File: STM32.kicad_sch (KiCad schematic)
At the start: 19 parts, among them IC1 TCAN3413DRBR, SW3 SW_SPDT, SW4 SW_Push, SW5 SW_SPDT, U1 STM32F072RBH6

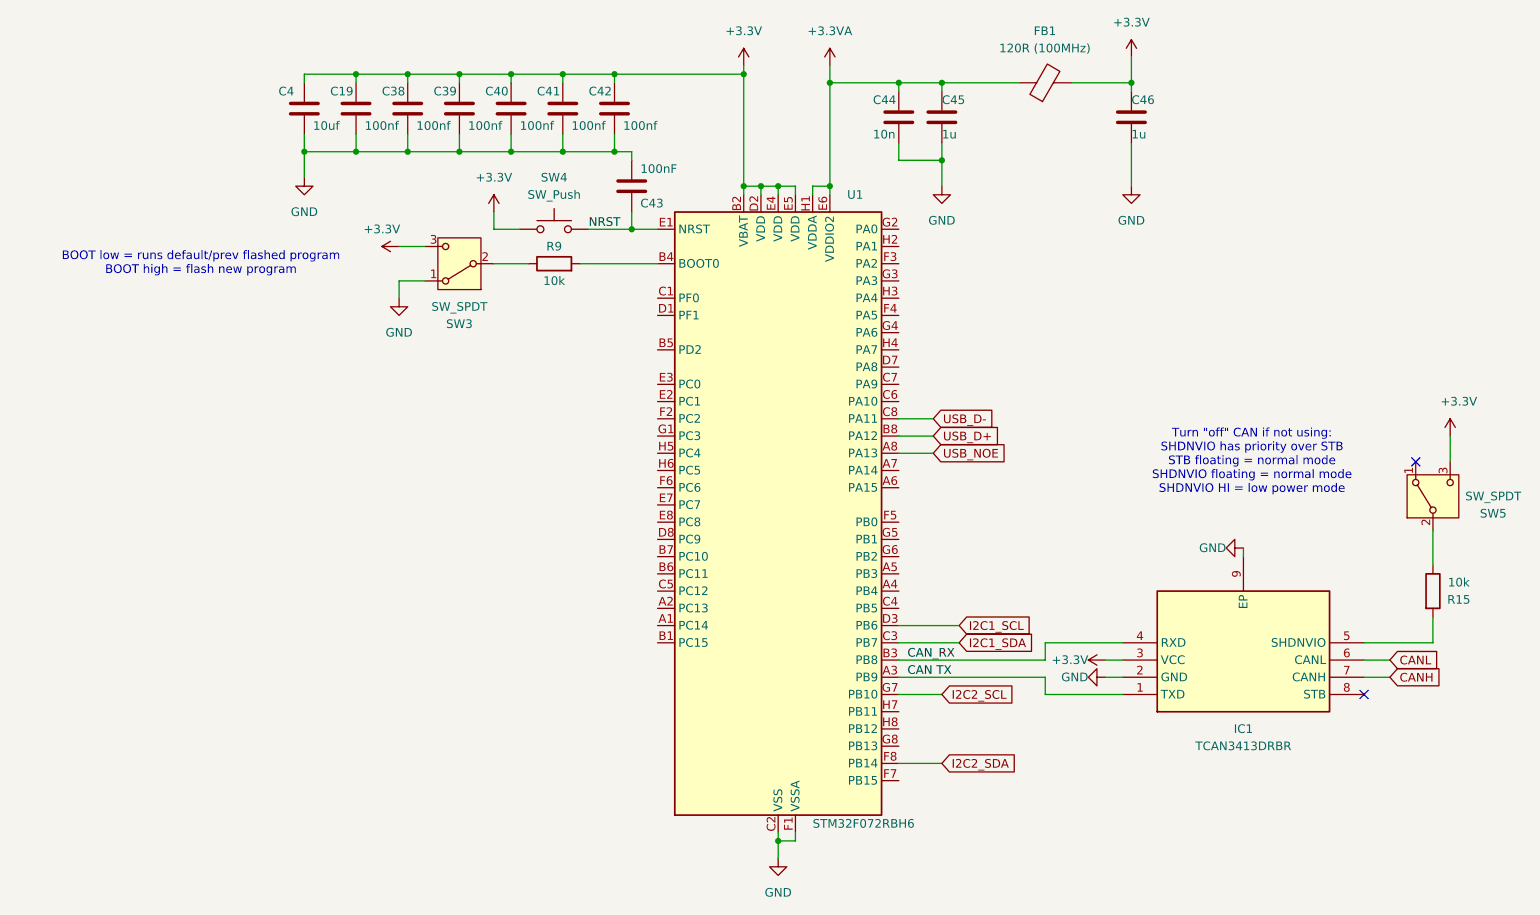
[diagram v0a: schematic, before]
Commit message: 3.3V changes and changed labels to hierarchical one's
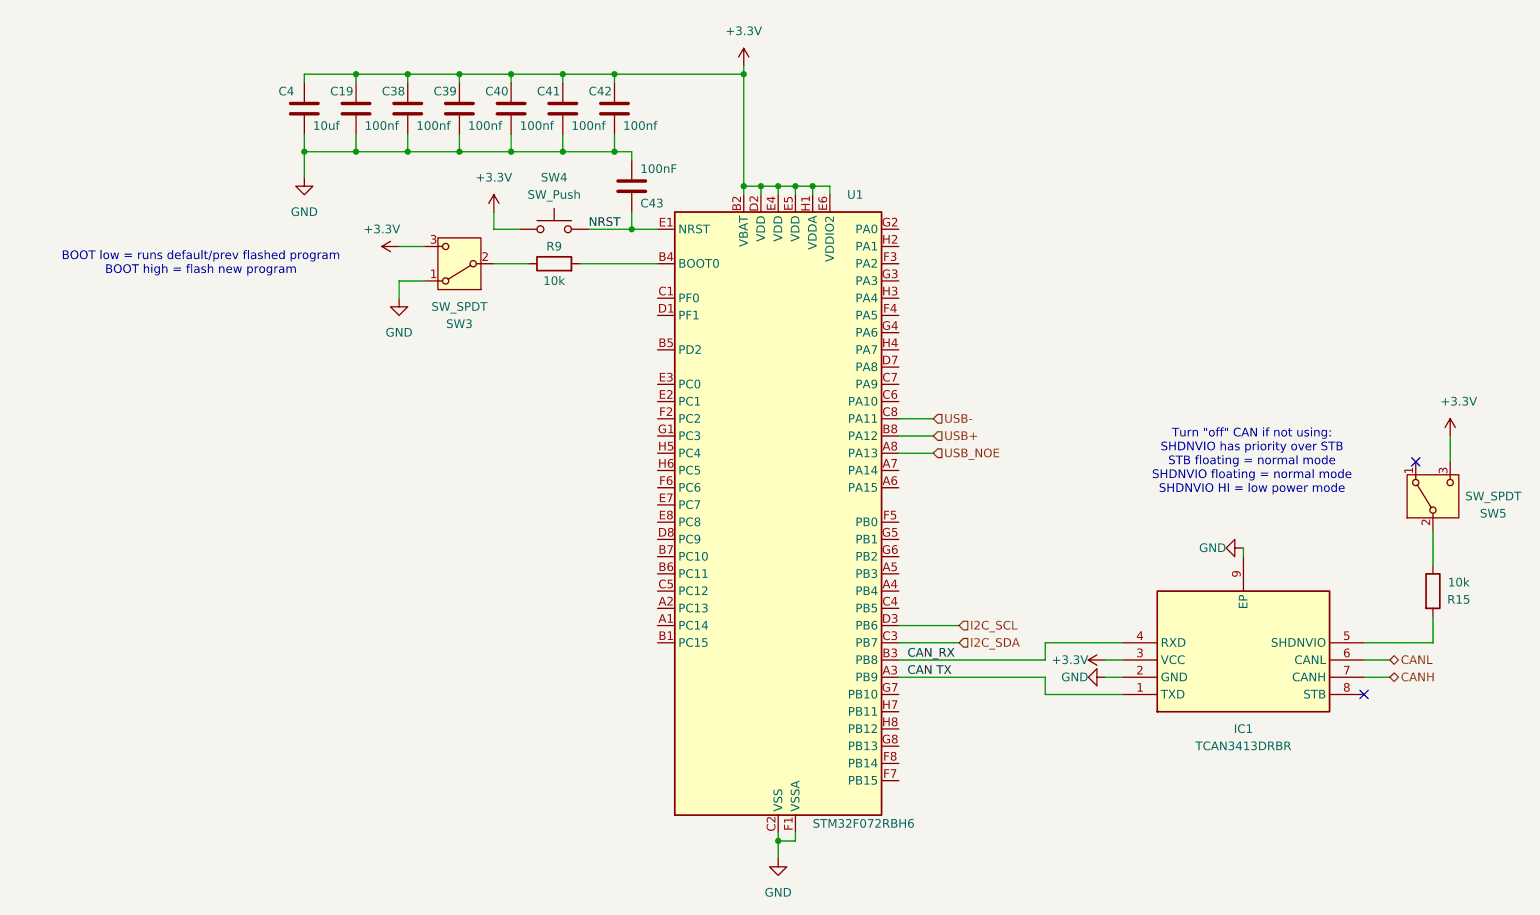
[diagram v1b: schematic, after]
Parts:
- removed C44: 10n, symbol Device:C
- removed C45, C46: 1u, symbol Device:C
- removed FB1: 120R (100MHz), symbol Device:FerriteBead
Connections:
- net +3.3VA is gone; now on net +3.3V: U1.E6 (VDDIO2), U1.H1 (VDDA)
- net I2C1_SCL renamed I2C_SCL
- net I2C1_SDA renamed I2C_SDA
- net I2C2_SCL: no longer names the net of U1.G7 (PB10)
- net I2C2_SDA: no longer names the net of U1.F8 (PB14)
- net USB_D+ renamed USB+
- net USB_D- renamed USB-

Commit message: linked everything together. still need to add capacitors
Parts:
- removed SW5: SW_SPDT, symbol Switch:SW_SPDT
- added D7: LED, symbol Device:LED
- added R17: 330, symbol Device:R_US
- R15, R9: symbol Device:R -> Device:R_US
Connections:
- net GND: now also D7.1 (K)
- net at U1.F5 (PB0): now also R15.1
- net USB_NOE: no longer names the net of U1.A8 (PA13)
- net USB_NOE: now also R17.2
- new net: D7.2 (A), R17.1
- no-connect marks 2 -> 1

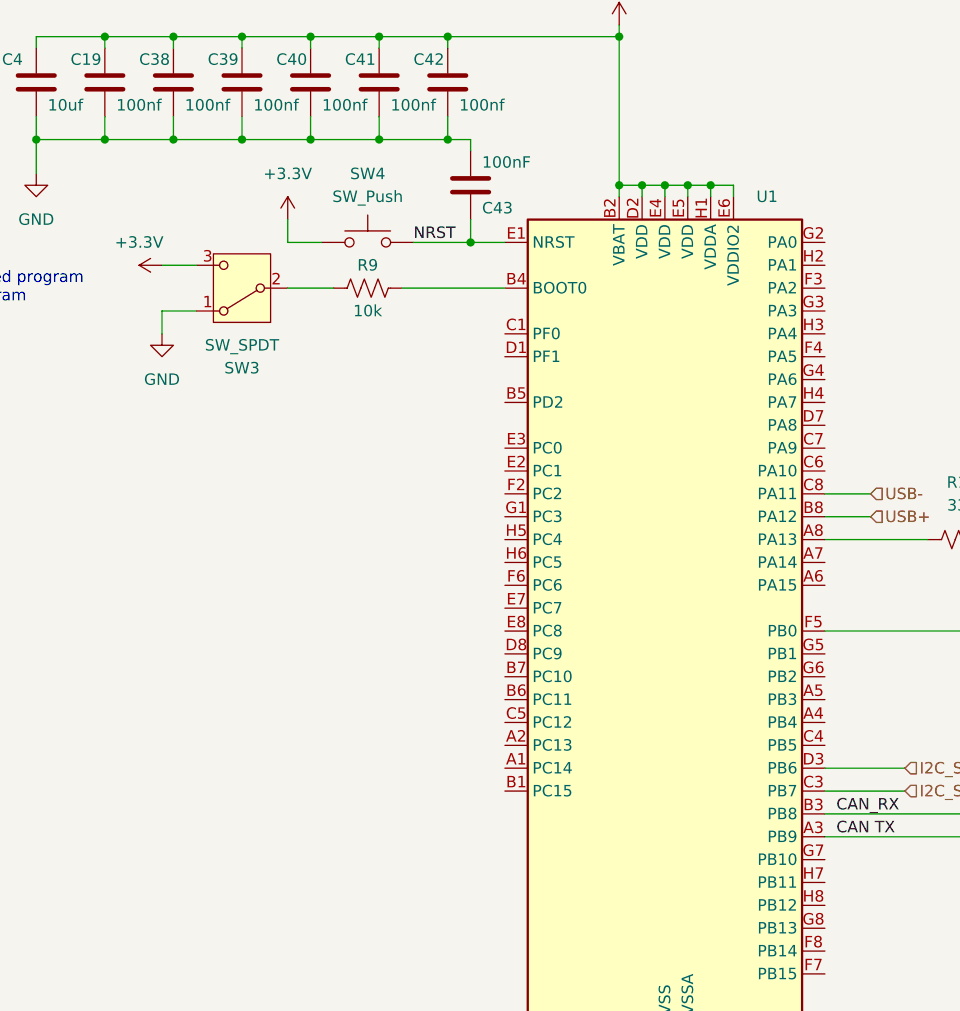
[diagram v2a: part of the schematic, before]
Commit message: started pcb layout, host and usbhub done
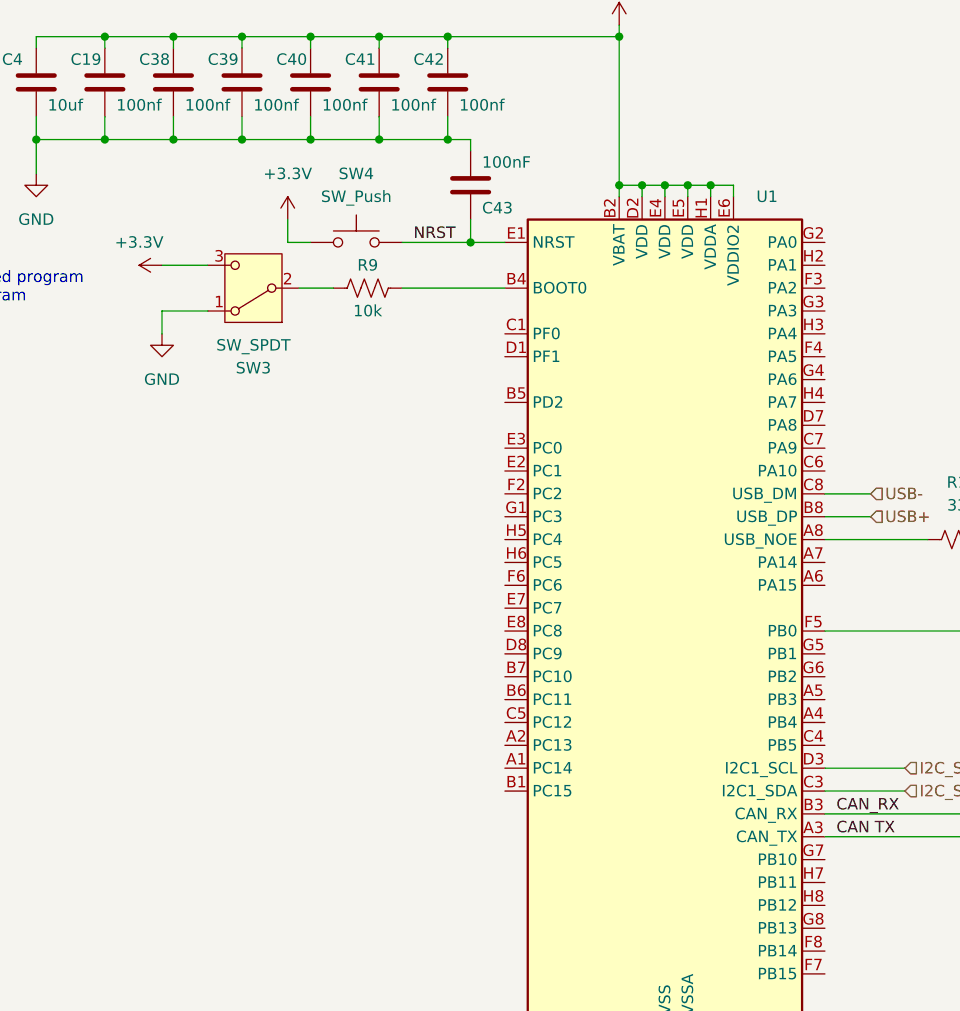
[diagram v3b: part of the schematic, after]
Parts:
- C19, C38, C39, C4, C40, C41, C42, C43: footprint (none) -> Capacitor_SMD:C_0603_1608Metric
- D7: footprint (none) -> LED_SMD:LED_0603_1608Metric
- R15, R17, R9: footprint (none) -> Resistor_SMD:R_0603_1608Metric
- SW3: footprint (none) -> Button_Switch_SMD:SW_SPDT_PCM12
- SW4: footprint (none) -> Button_Switch_SMD:SW_Push_1P1T_XKB_TS-1187A
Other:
- moved on the sheet: SW3, SW4
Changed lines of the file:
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@@
 	(wire
 		(pts
-			(xy 132.08 64.77) (xy 137.16 64.77)
+			(xy 133.35 64.77) (xy 137.16 64.77)
 		)
 		(stroke
@@
 	(wire
 		(pts
-			(xy 118.11 62.23) (xy 121.92 62.23)
+			(xy 118.11 62.23) (xy 123.19 62.23)
 		)
 		(stroke
@@
 	(wire
 		(pts
-			(xy 135.89 59.69) (xy 132.08 59.69)
+			(xy 134.62 59.69) (xy 132.08 59.69)
 		)
 		(stroke
@@
 	(wire
 		(pts
-			(xy 118.11 67.31) (xy 121.92 67.31)
+			(xy 118.11 67.31) (xy 123.19 67.31)
 		)
 		(stroke
@@
 	(wire
 		(pts
-			(xy 146.05 59.69) (xy 152.4 59.69)
+			(xy 144.78 59.69) (xy 152.4 59.69)
 		)
 		(stroke
@@
 		)
 		(pin "A3"
+			(alternate "CAN_TX")
 		)
 		(pin "F3"
@@
 		)
 		(pin "C3"
+			(alternate "I2C1_SDA")
 		)
 		(pin "G6"
@@
 		)
 		(pin "B8"
+			(alternate "USB_DP")
 		)
 		(pin "C2"
 		)
 		(pin "A8"
+			(alternate "USB_NOE")
 		)
 		(pin "C4"
@@
 		)
 		(pin "C8"
+			(alternate "USB_DM")
 		)
 		(pin "C7"
 		)
 		(pin "D3"
+			(alternate "I2C1_SCL")
 		)
 		(pin "E1"
@@
 		)
 		(pin "B3"
+			(alternate "CAN_RX")
 		)
 		(pin "A2"
@@
 			)
 		)
-		(property "Footprint" ""
+		(property "Footprint" "Capacitor_SMD:C_0603_1608Metric"
 			(at 105.1052 45.72 0)
 			(effects
@@
 	(symbol
 		(lib_id "Switch:SW_Push")
-		(at 140.97 59.69 0)
+		(at 139.7 59.69 0)
 		(unit 1)
 		(exclude_from_sim no)
@@
 		(fields_autoplaced yes)
 		(property "Reference" "SW4"
-			(at 140.97 52.07 0)
+			(at 139.7 52.07 0)
 			(effects
 				(font
@@
 		)
 		(property "Value" "SW_Push"
-			(at 140.97 54.61 0)
-			(effects
-				(font
-					(size 1.27 1.27)
-				)
-			)
-		)
-		(property "Footprint" ""
-			(at 140.97 54.61 0)
+			(at 139.7 54.61 0)
+			(effects
+				(font
+					(size 1.27 1.27)
+				)
+			)
+		)
+		(property "Footprint" "Button_Switch_SMD:SW_Push_1P1T_XKB_TS-1187A"
+			(at 139.7 54.61 0)
 			(effects
 				(font
@@
 		)
 		(property "Datasheet" "~"
-			(at 140.97 54.61 0)
+			(at 139.7 54.61 0)
 			(effects
 				(font
@@
 		)
 		(property "Description" "Push button switch, generic, two pins"
-			(at 140.97 59.69 0)
+			(at 139.7 59.69 0)
 			(effects
 				(font
@@
 			)
 		)
-		(property "Footprint" ""
+		(property "Footprint" "LED_SMD:LED_0603_1608Metric"
 			(at 214.63 92.71 0)
 			(effects
@@
 			)
 		)
-		(property "Footprint" ""
+		(property "Footprint" "Resistor_SMD:R_0603_1608Metric"
 			(at 206.756 93.726 90)
 			(effects
@@
 	(symbol
 		(lib_id "Switch:SW_SPDT")
-		(at 127 64.77 180)
+		(at 128.27 64.77 180)
 		(unit 1)
 		(exclude_from_sim no)
@@
 		(dnp no)
 		(property "Reference" "SW3"
-			(at 127 73.66 0)
+			(at 128.27 73.66 0)
 			(effects
 				(font
@@
 		)
 		(property "Value" "SW_SPDT"
-			(at 127 71.12 0)
-			(effects
-				(font
-					(size 1.27 1.27)
-				)
-			)
-		)
-		(property "Footprint" ""
-			(at 127 64.77 0)
+			(at 128.27 71.12 0)
+			(effects
+				(font
+					(size 1.27 1.27)
+				)
+			)
+		)
+		(property "Footprint" "Button_Switch_SMD:SW_SPDT_PCM12"
+			(at 128.27 64.77 0)
 			(effects
 				(font
@@
 		)
 		(property "Datasheet" "~"
-			(at 127 57.15 0)
+			(at 128.27 57.15 0)
 			(effects
 				(font
@@
 		)
 		(property "Description" "Switch, single pole double throw"
-			(at 127 64.77 0)
+			(at 128.27 64.77 0)
 			(effects
 				(font
@@
 			)
 		)
-		(property "Footprint" ""
+		(property "Footprint" "Capacitor_SMD:C_0603_1608Metric"
 			(at 150.8252 45.72 0)
 			(effects
@@
 			)
 		)
-		(property "Footprint" ""
+		(property "Footprint" "Capacitor_SMD:C_0603_1608Metric"
 			(at 120.3452 45.72 0)
 			(effects
@@
 			)
 		)
-		(property "Footprint" ""
+		(property "Footprint" "Capacitor_SMD:C_0603_1608Metric"
 			(at 153.3652 57.15 0)
 			(effects
@@
 			)
 		)
-		(property "Footprint" ""
+		(property "Footprint" "Capacitor_SMD:C_0603_1608Metric"
 			(at 127.9652 45.72 0)
 			(effects
@@
 			)
 		)
-		(property "Footprint" ""
+		(property "Footprint" "Capacitor_SMD:C_0603_1608Metric"
 			(at 143.2052 45.72 0)
 			(effects
@@
 			)
 		)
-		(property "Footprint" ""
+		(property "Footprint" "Resistor_SMD:R_0603_1608Metric"
 			(at 141.224 63.754 90)
 			(effects
@@
 			)
 		)
-		(property "Footprint" ""
+		(property "Footprint" "Capacitor_SMD:C_0603_1608Metric"
 			(at 135.5852 45.72 0)
 			(effects
@@
 			)
 		)
-		(property "Footprint" ""
+		(property "Footprint" "Resistor_SMD:R_0603_1608Metric"
 			(at 271.526 113.284 90)
 			(effects
@@
 			)
 		)
-		(property "Footprint" ""
+		(property "Footprint" "Capacitor_SMD:C_0603_1608Metric"
 			(at 112.7252 45.72 0)
 			(effects

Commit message: routed stm32
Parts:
- removed C41, C42: 100nf, Capacitor_SMD:C_0603_1608Metric, symbol Device:C
- removed D7: LED, LED_SMD:LED_0603_1608Metric, symbol Device:LED
- removed R17: 330, Resistor_SMD:R_0603_1608Metric, symbol Device:R_US
- removed SW3: SW_SPDT, Button_Switch_SMD:SW_SPDT_PCM12, symbol Switch:SW_SPDT
- added C50, C51: 4.7uF, Capacitor_SMD:C_0603_1608Metric, symbol Device:C
- added C52: 1uF, Capacitor_SMD:C_0603_1608Metric, symbol Device:C
- added SW3: SW_Push, Button_Switch_SMD:SW_Push_1P1T_XKB_TS-1187A, symbol Switch:SW_Push
- U1: footprint Package_BGA:UFBGA-64_5x5mm_Layout8x8_P0.5mm -> Package_QFP:LQFP-64_10x10mm_P0.5mm; symbol MCU_ST_STM32F0:STM32F072RBHx -> MCU_ST_STM32F0:STM32F072RBTx
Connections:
- net +3.3V: now also U1.1 (VBAT), U1.13 (VDDA), U1.19 (VDD), U1.32 (VDD), U1.48 (VDDIO2), U1.64 (VDD), C50.1, C51.1, C52.1, SW3.1; no longer U1.B2 (VBAT), U1.D2 (VDD), U1.E4 (VDD), U1.E5 (VDD), U1.E6 (VDDIO2), U1.H1 (VDDA)
- net CAN TX: now also U1.62 (PB9); no longer U1.A3 (PB9)
- net CAN_RX: now also U1.61 (PB8); no longer U1.B3 (PB8)
- net GND: now also R9.2, U1.12 (VSSA), U1.18 (VSS), U1.31 (VSS), U1.47 (VSS), U1.60 (BOOT0), U1.63 (VSS), C50.2, C51.2, C52.2; no longer U1.C2 (VSS), U1.D4 (VSS), U1.D5 (VSS), U1.D6 (VSS), U1.F1 (VSSA)
- net I2C_SCL: now also U1.58 (PB6); no longer U1.D3 (PB6)
- net I2C_SDA: now also U1.59 (PB7); no longer U1.C3 (PB7)
- net NRST: now also U1.7 (NRST); no longer U1.E1 (NRST)
- net USB+: now also U1.45 (PA12); no longer U1.B8 (PA12)
- net USB-: now also U1.44 (PA11); no longer U1.C8 (PA11)
- net at R15.1: now also U1.49 (PA14); no longer U1.F5 (PB0)
- net at R9.1: now also SW3.2
- no-connect marks 1 -> 45
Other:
- moved on the sheet: R9, SW4

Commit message: pcb routed!!!!!!!
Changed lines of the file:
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@@
 		)
 		(pin "14"
-			(alternate "CAN_TX")
 		)
 		(pin "62"
+			(alternate "CAN_TX")
 		)
 		(pin "57"
@@
 		)
 		(pin "61"
-			(alternate "I2C1_SDA")
+			(alternate "CAN_RX")
 		)
 		(pin "10"
 		)
 		(pin "25"
-			(alternate "I2C2_SCL")
+			(alternate "PC5")
 		)
 		(pin "33"
 		)
 		(pin "59"
+			(alternate "I2C1_SDA")
 		)
 		(pin "26"
@@
 		)
 		(pin "45"
+			(alternate "USB_DP")
 		)
 		(pin "28"
-			(alternate "USB_DP")
+			(alternate "PB2")
 		)
 		(pin "58"
+			(alternate "I2C1_SCL")
 		)
 		(pin "21"
-			(alternate "USB_NOE")
+			(alternate "PA5")
 		)
 		(pin "36"
@@
 		)
 		(pin "29"
-			(alternate "USB_DM")
+			(alternate "PB10")
 		)
 		(pin "19"
 		)
 		(pin "53"
-			(alternate "I2C1_SCL")
+			(alternate "PC12")
 		)
 		(pin "54"
@@
 		)
 		(pin "44"
+			(alternate "USB_DM")
 		)
 		(pin "17"
@@
 		)
 		(pin "20"
-			(alternate "CAN_RX")
+			(alternate "PA4")
 		)
 		(pin "9"
